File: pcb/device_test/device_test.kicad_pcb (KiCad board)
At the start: 4 copper layers, 55.9 x 55.9 mm, 18 parts, among them J101 Screw_Terminal_01x02, J201 Conn_01x05, J202 USB_C_Receptacle_USB2.0_16P, J203 Conn_01x04, J204 Conn_01x08, J301 Conn_01x05, J302 USB_A, J303 Conn_01x06

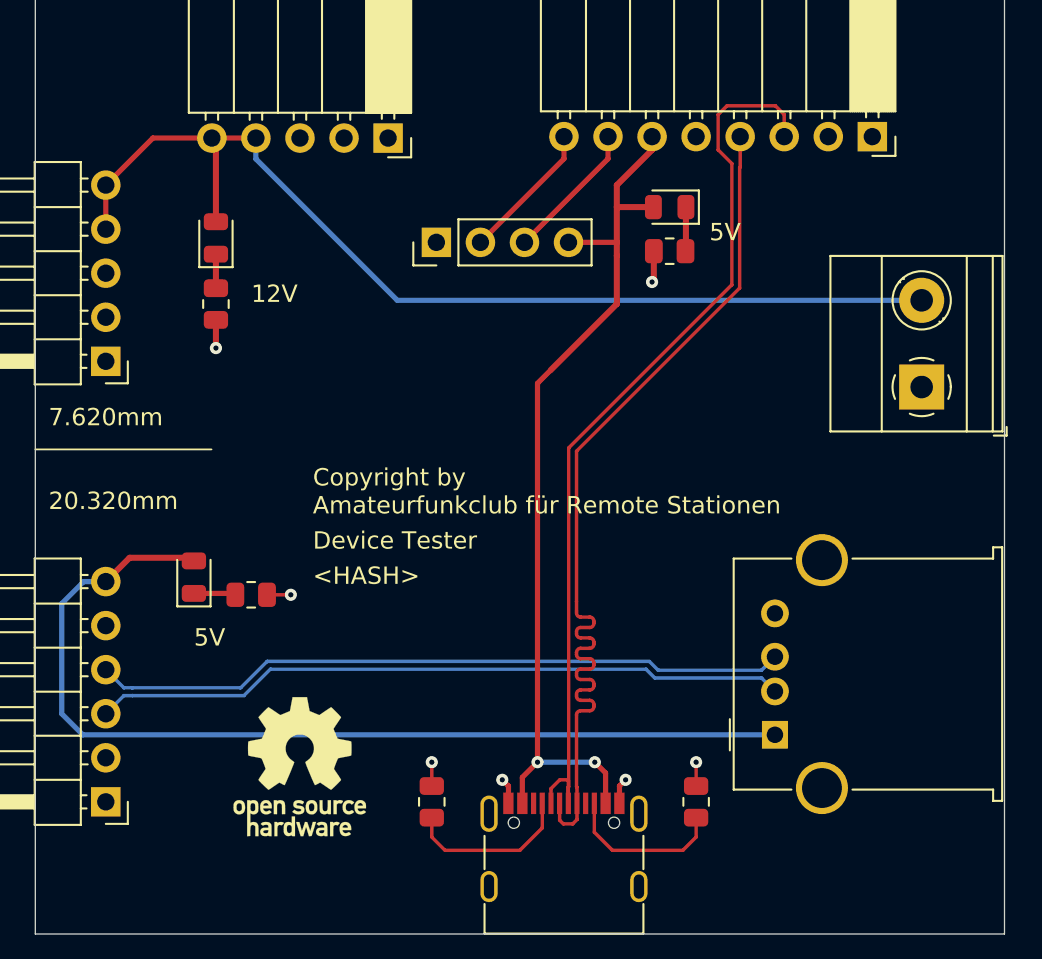
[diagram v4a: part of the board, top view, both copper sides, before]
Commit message: remove usb a, add usb c
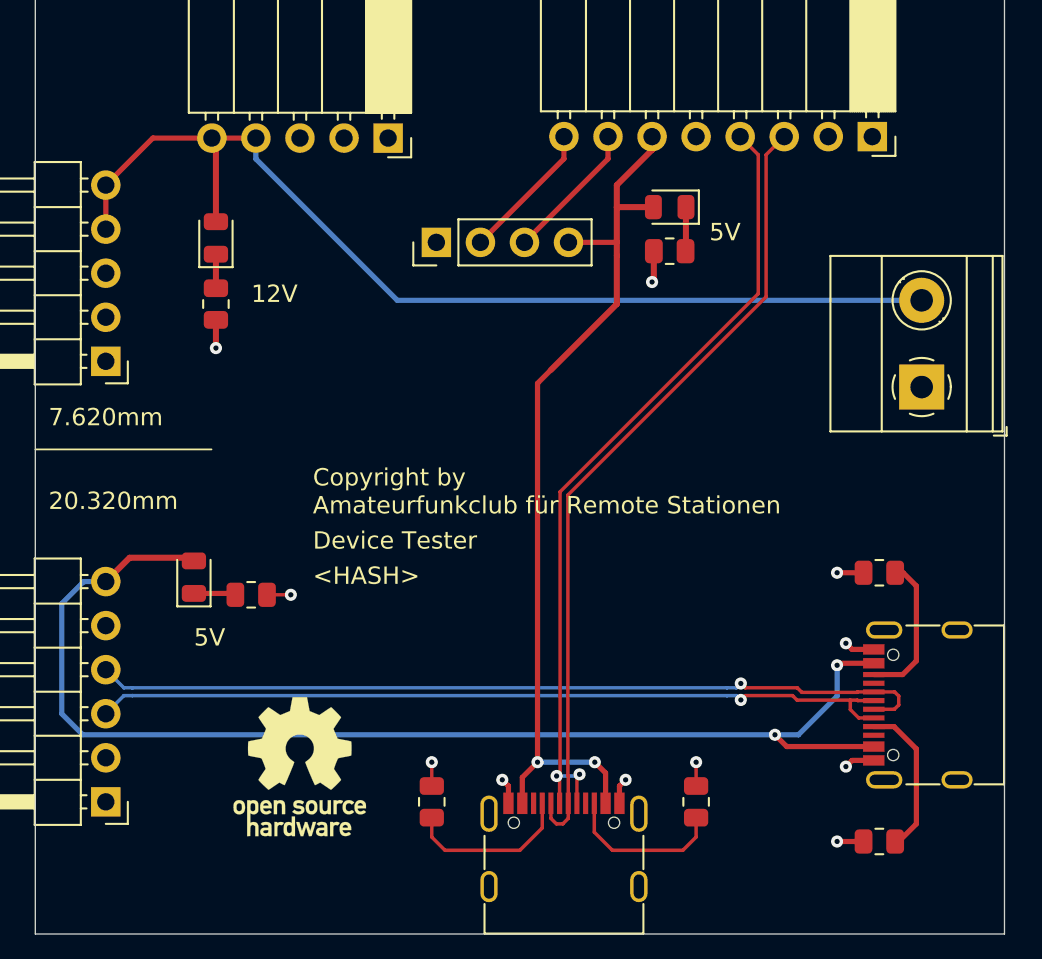
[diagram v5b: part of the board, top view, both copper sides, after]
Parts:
- added R302: 5k1, Resistor_SMD:R_0805_2012Metric, F.Cu at (164.4, 113.8)
- added R303: 5k1, Resistor_SMD:R_0805_2012Metric, F.Cu at (164.4, 98.3)
- J302: value USB_A -> USB_C_Receptacle_USB2.0_16P; footprint Connector_USB:USB_A_Molex_67643_Horizontal -> Connector_USB:USB_C_Receptacle_G-Switch_GT-USB-7010ASV
- moved J302 9.58 mm to (167.8, 105.9)
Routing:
- net +5V_B: track 56.4 -> 70.9 mm, vias 0 -> 2
- net /Bus Tester Connector/CC1: track 0.00 -> 8.95 mm
- net /Bus Tester Connector/CC2: track 0.00 -> 8.64 mm
- net /Bus Tester Connector/USB+: track 40.2 -> 48.6 mm, vias 0 -> 1
- net /Bus Tester Connector/USB-: track 40.2 -> 47.1 mm, vias 0 -> 1
- net GND: track 10.6 -> 17.1 mm, vias 7 -> 11
- net /Device Tester Connector/USB+: track 53.2 -> 46.7 mm, vias 0 -> 2
- net /Device Tester Connector/USB-: track 52.9 -> 46.6 mm

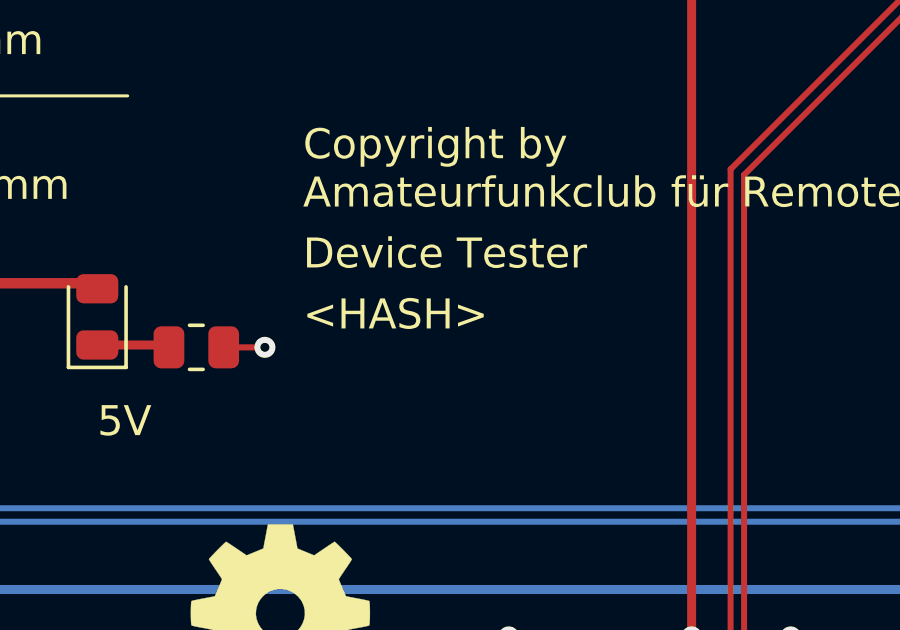
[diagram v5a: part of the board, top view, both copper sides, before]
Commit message: add correct HASH tag to pcb
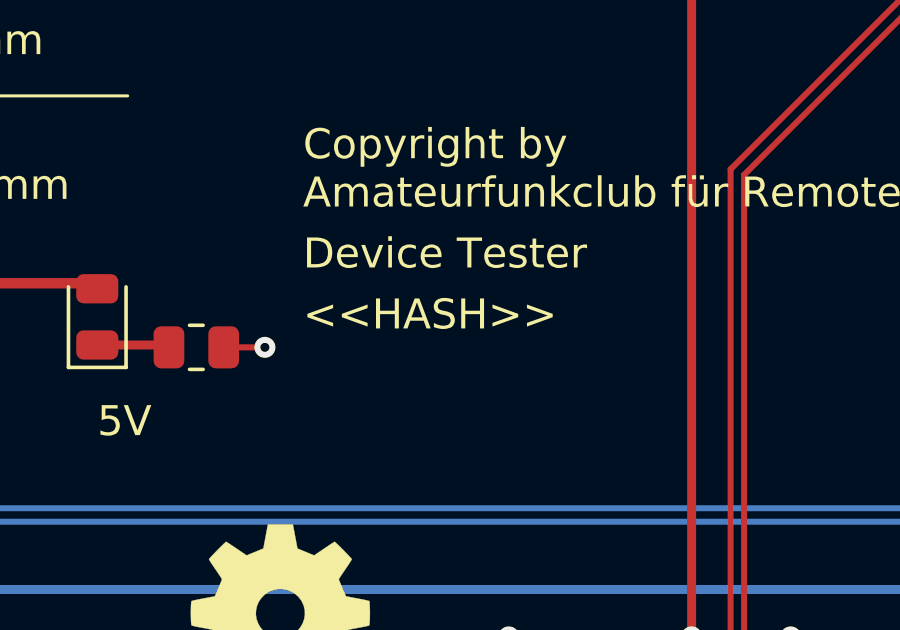
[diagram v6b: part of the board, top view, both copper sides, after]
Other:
- board text added: "<<HASH>>"
- board text removed: "<HASH>"
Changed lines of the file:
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@@
 		)
 	)
-	(gr_text "<HASH>"
-		(at 158.682 93.726 -0)
+	(gr_text "<<HASH>>"
+		(at 158.682 93.726 0)
 		(layer "B.SilkS")
 		(effects
@@
 		)
 	)
-	(gr_text "<HASH>"
+	(gr_text "<<HASH>>"
 		(at 131.758 99.06 0)
 		(layer "F.SilkS")

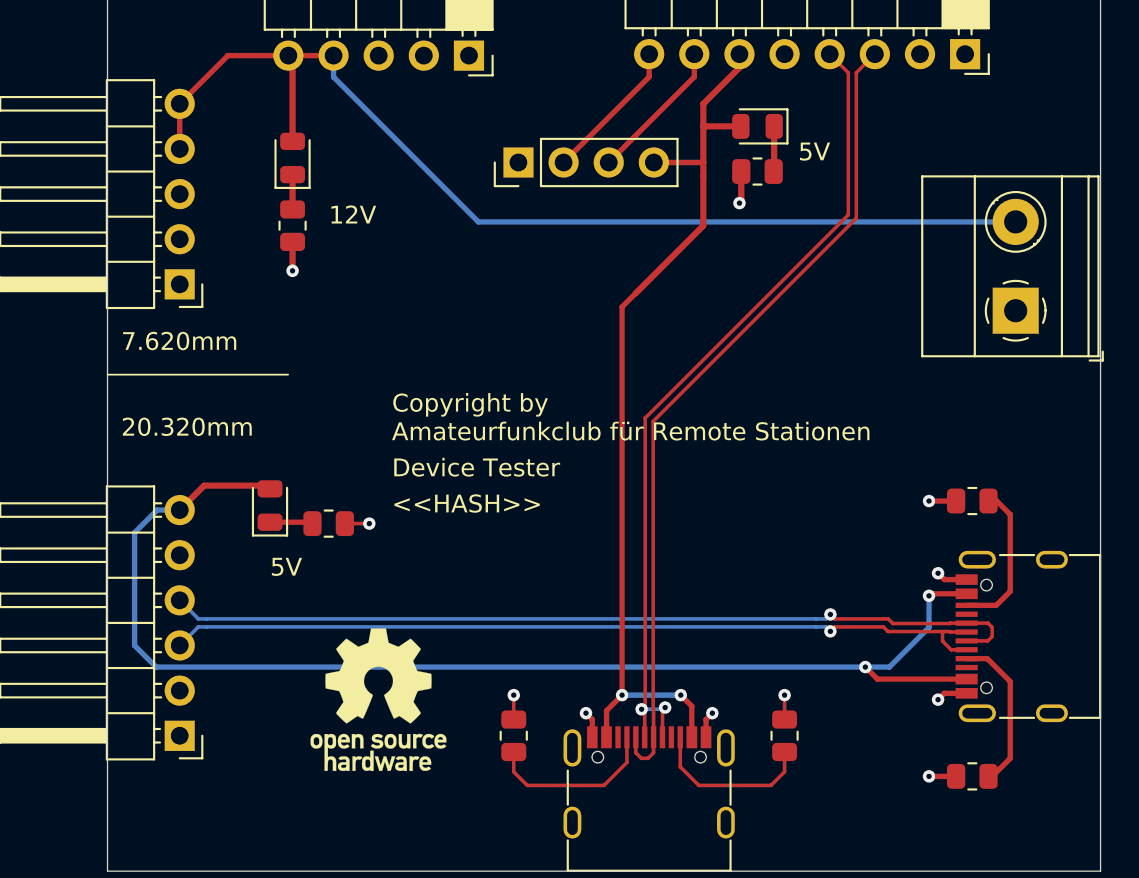
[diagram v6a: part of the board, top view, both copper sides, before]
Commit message: added more information on PCB
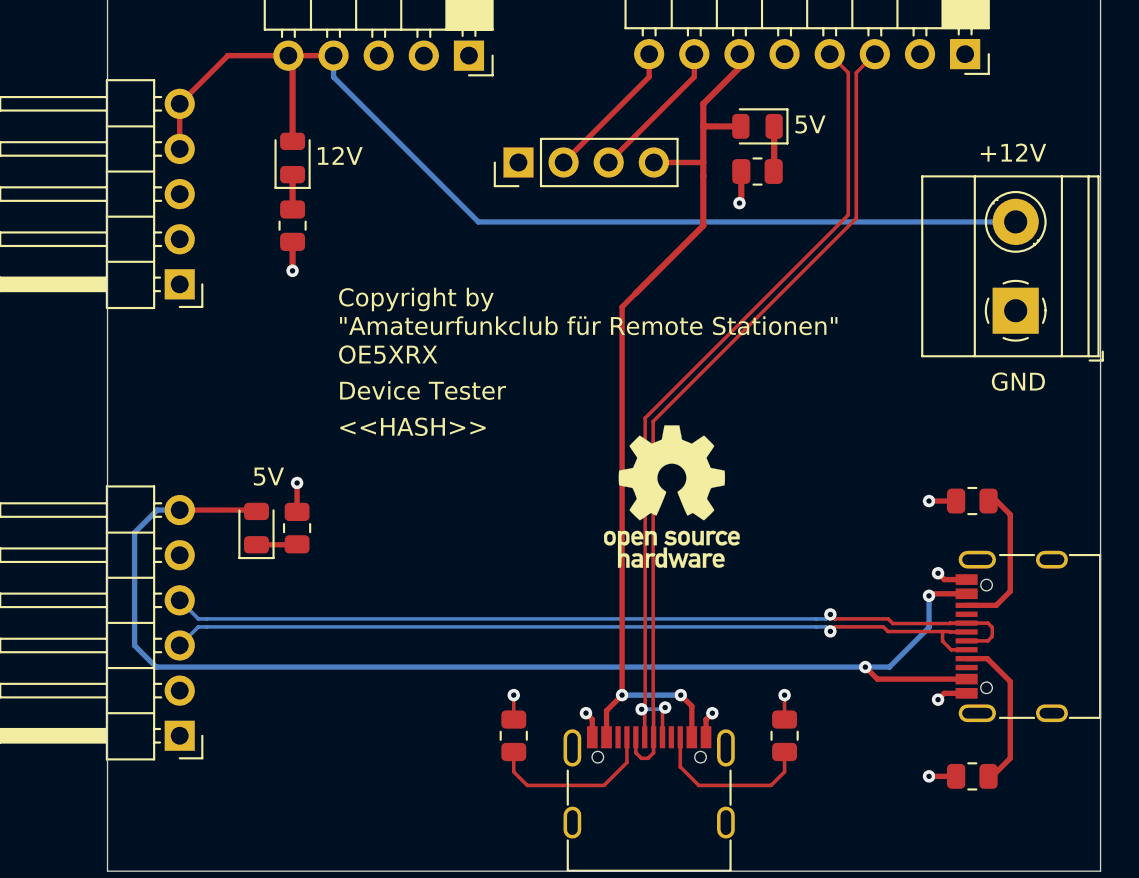
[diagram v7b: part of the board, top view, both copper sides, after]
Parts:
- moved #SYM101 34.9 mm to (155.1, 84.3), turned to 0 degrees
- moved #SYM101 20.1 mm to (147.5, 98.0)
- moved R301 1.80 mm to (126.4, 99.8), turned to 90 degrees
- moved D301 1.48 mm to (124.1, 99.8)
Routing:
- net +5V_B: track 70.9 -> 69.8 mm
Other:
- board text added: "+12V"
- board text added: "+12V GND"
- board text added: "+5V"
- board text added: "Copyright by {dblquote}Amateurfunkclub für Remote Stationen{dblquote} OE5XRX"
- board text added: "GND"
- board text added: "USB+"
- board text added: "USB-"
- board text added: "USB_OTG"
- board text added: "nRPIBOOT"
- board text removed: "20.320mm"
- board text removed: "7.620mm"
- board text removed: "Copyright by Amateurfunkclub für Remote Stationen"
